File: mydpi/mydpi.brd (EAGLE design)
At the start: 41 x 20 mm, 35 parts, among them Q1 DMN3404L, U1 MEGA32U4-MU, U2 RT9193-33GB, Y1 830069392

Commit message: Minor changes placement
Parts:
- removed C6: 100n, zaan-Capacitors:C0603
- moved Q1 3.54 mm to (31.8, 12.2), turned to 90 degrees
- moved R4 3.26 mm to (32.5, 15.8), turned to 270 degrees
- moved SJ1 2.69 mm to (10.5, 28.5), turned to 180 degrees
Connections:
- removed net MEDBG_VTG: DBG1.4, SJ1.2
- new net VTG: C10.1, C11.1, C7.1, DBG1.4, SJ1.2
- net +3V3: no longer C10.1, C11.1
- net +5V: no longer C6.1, C7.1
- net GND: no longer C6.2
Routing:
- net PE6: track 19.5 -> 2.94 mm, vias 2 -> 1
- net MEDBG_UPDI: track 4.63 -> 0.00 mm
- net +3V3: track 3.74 -> 0.00 mm
- net VTG: track 0.00 -> 3.64 mm
- net GND: track 48.2 -> 46.0 mm, vias 30 -> 28
- net N$3: track 1.50 -> 0.00 mm

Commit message: Bugfixes in used libraries
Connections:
- removed net MEDBG_UPDI: DBG1.3, R4.2
- new net N$3: R4.2
- new net UDPI: DBG1.3
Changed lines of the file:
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@@
 </attributes>
 <variantdefs>
+<variantdef name="BOM"/>
 </variantdefs>
 <classes>
@@
 <attribute name="VOLTAGE" value="75V" x="25.75" y="16" size="1.778" layer="27" rot="R90" display="off"/>
 </element>
-<element name="ICSP1" library="zaan-Connectors" library_urn="urn:adsk.eagle:library:16759010" package="AVRISP-1.27-SMD" value="AVR-ISP-SMD" x="14.5" y="5.5" smashed="yes" rot="MR180">
+<element name="ICSP1" library="zaan-Connectors" library_urn="urn:adsk.eagle:library:16759010" package="AVRISP-1.27-SMD" package3d_urn="urn:adsk.eagle:package:17075154/1" value="AVR-ISP-SMD" x="14.5" y="5.5" smashed="yes" rot="MR180">
 <attribute name="NAME" x="17" y="5.5" size="1.016" layer="26" font="vector" ratio="15" rot="MR90" align="center"/>
 </element>
@@
 </element>
 <element name="Y1" library="zaan-Electromechanical" library_urn="urn:adsk.eagle:library:16759157" package="WE-XTAL_CFPX-218" package3d_urn="urn:adsk.eagle:package:16759170/1" value="830069392" x="22.5" y="2.75" smashed="yes" rot="R180">
+<attribute name="DESCRIPTION" value="Crystal" x="22.5" y="2.75" size="1.778" layer="27" rot="R180" display="off"/>
+<attribute name="MF" value="Wurth Electronics" x="22.5" y="2.75" size="1.778" layer="27" rot="R180" display="off"/>
+<attribute name="MPN" value="830069392" x="22.5" y="2.75" size="1.778" layer="27" rot="R180" display="off"/>
 <attribute name="NAME" x="22.5" y="5" size="1.016" layer="25" font="vector" ratio="15" align="center"/>
+<attribute name="PACKAGE" value="2520" x="22.5" y="2.75" size="1.778" layer="27" rot="R180" display="off"/>
 <attribute name="VALUE" x="22.5" y="5.25" size="1.016" layer="27" font="vector" ratio="15" rot="R180" align="center"/>
 </element>
@@
 </element>
 <element name="S1" library="zaan-Electromechanical" library_urn="urn:adsk.eagle:library:16759157" package="SPST-6X3.6" package3d_urn="urn:adsk.eagle:package:16760026/2" value="TS-1101-C-W" x="29.75" y="5.75" smashed="yes" rot="R270">
+<attribute name="DESCRIPTION" value="Tactile Button" x="29.75" y="5.75" size="1.778" layer="27" rot="R270" display="off"/>
+<attribute name="MF" value="Korean Hroparts Elec" x="29.75" y="5.75" size="1.778" layer="27" rot="R270" display="off"/>
+<attribute name="MPN" value="K2-1107ST-A4SW-06" x="29.75" y="5.75" size="1.778" layer="27" rot="R270" display="off"/>
 <attribute name="NAME" x="28.25" y="9.75" size="1.016" layer="25" font="vector" ratio="15" rot="R270" align="center"/>
+<attribute name="PACKAGE" value="6.1X3.6X2.5" x="29.75" y="5.75" size="1.778" layer="27" rot="R270" display="off"/>
 <attribute name="VALUE" x="27.25" y="5.75" size="1.016" layer="27" font="vector" ratio="15" rot="R270" align="center"/>
 </element>
@@
 <attribute name="MPN" value="MF-PSMF035X-2" x="9.25" y="6.5" size="1.778" layer="27" rot="R270" display="off"/>
 <attribute name="NAME" x="9.25" y="4" size="1.016" layer="25" font="vector" ratio="15" rot="R270" align="center"/>
-<attribute name="PACKAGE" value="0805" x="9.25" y="6.5" size="1.778" layer="27" rot="R270" display="off"/>
+<attribute name="PACKAGE" value="2012" x="9.25" y="6.5" size="1.778" layer="27" rot="R270" display="off"/>
 <attribute name="VALUE" x="5.75" y="6.5" size="1.016" layer="27" font="vector" ratio="15" rot="R270" align="center"/>
 </element>
@@
 <wire x1="8.5" y1="14.65" x2="7.5" y2="14.65" width="0.254" layer="1"/>
 <via x="7.5" y="14.65" extent="1-16" drill="0.3"/>
+<wire x1="33.25" y1="7.25" x2="38.77" y2="11.905" width="0" layer="19" extent="1-1"/>
+<wire x1="29.75" y1="8.25" x2="32.25" y2="7.25" width="0" layer="19" extent="1-1"/>
+<wire x1="27.5" y1="7.25" x2="29.75" y2="8.25" width="0" layer="19" extent="1-1"/>
+<wire x1="20.5" y1="10" x2="22.75" y2="7.75" width="0" layer="19" extent="1-1"/>
+<wire x1="22.5" y1="12" x2="20.5" y2="10" width="0" layer="19" extent="1-1"/>
+<wire x1="19.5" y1="17" x2="21.5" y2="17" width="0" layer="19" extent="1-1"/>
+<wire x1="17.025" y1="10.5" x2="18.5" y2="12" width="0" layer="19" extent="1-1"/>
+<wire x1="21.5375" y1="3.5125" x2="19.498" y2="5.75" width="0" layer="19" extent="1-1"/>
+<wire x1="22.5125" y1="1.9875" x2="22.4875" y2="3.5125" width="0" layer="19" extent="1-1"/>
+<wire x1="25.5" y1="1.9" x2="23.4625" y2="1.9875" width="0" layer="19" extent="1-1"/>
+<wire x1="19.5" y1="1.9" x2="21.5375" y2="3.5125" width="0" layer="19" extent="1-1"/>
+<wire x1="17.5" y1="1.9" x2="19.5" y2="1.9" width="0" layer="19" extent="1-1"/>
+<wire x1="15.5" y1="2.75" x2="17.5" y2="1.9" width="0" layer="19" extent="1-1"/>
+<wire x1="15.135" y1="6.77" x2="15.5" y2="3.65" width="0" layer="19" extent="1-16"/>
+<wire x1="14.5" y1="13.75" x2="15.75" y2="10.398" width="0" layer="19" extent="1-1"/>
+<wire x1="11.25" y1="15.5" x2="14.5" y2="14.65" width="0" layer="19" extent="1-1"/>
+<wire x1="8.5" y1="14.65" x2="10.21" y2="15.5" width="0" layer="19" extent="1-1"/>
+<wire x1="7.725" y1="13.225" x2="7.5" y2="14.65" width="0" layer="19" extent="1-1"/>
+<wire x1="6.25" y1="16" x2="7.5" y2="14.65" width="0" layer="19" extent="1-1"/>
+<wire x1="12.75" y1="18" x2="11.25" y2="15.5" width="0" layer="19" extent="1-1"/>
+<wire x1="11.25" y1="6.15" x2="15.135" y2="6.77" width="0" layer="19" extent="1-16"/>
+<wire x1="7.725" y1="6.775" x2="11.25" y2="6.15" width="0" layer="19" extent="1-1"/>
+<wire x1="6.25" y1="4" x2="6.51" y2="6.775" width="0" layer="19" extent="1-1"/>
+<wire x1="6.5" y1="1.75" x2="6.25" y2="4" width="0" layer="19" extent="1-1"/>
+<wire x1="1.95" y1="18.5" x2="5.35" y2="16" width="0" layer="19" extent="1-1"/>
 </signal>
 <signal name="+5V">
@@
 <wire x1="14.5" y1="3.595" x2="14.5" y2="3.23" width="0.254" layer="16"/>
 <via x="14.5" y="3.23" extent="1-16" drill="0.3"/>
-<wire x1="8.35" y1="18.5" x2="13" y2="28" width="0" layer="19" extent="1-1"/>
+<wire x1="25.75" y1="16.85" x2="29.75" y2="14.95" width="0" layer="19" extent="1-1"/>
+<wire x1="23.6" y1="16" x2="25.75" y2="16.85" width="0" layer="19" extent="1-1"/>
+<wire x1="19" y1="13.475" x2="23" y2="13.475" width="0" layer="19" extent="1-1"/>
+<wire x1="18" y1="13.475" x2="19" y2="13.475" width="0" layer="19" extent="1-1"/>
+<wire x1="17.025" y1="12" x2="18" y2="13.475" width="0" layer="19" extent="1-1"/>
+<wire x1="17.025" y1="9.5" x2="17.025" y2="12" width="0" layer="19" extent="1-1"/>
+<wire x1="19" y1="6.525" x2="17.025" y2="9.5" width="0" layer="19" extent="1-1"/>
+<wire x1="17.5" y1="3.6" x2="19" y2="6.525" width="0" layer="19" extent="1-1"/>
+<wire x1="15.135" y1="4.23" x2="17.5" y2="3.6" width="0" layer="19" extent="1-16"/>
+<wire x1="13.5" y1="3.65" x2="14.5" y2="3.23" width="0" layer="19" extent="1-1"/>
+<wire x1="9.45" y1="1.75" x2="13.5" y2="3.65" width="0" layer="19" extent="1-1"/>
+<wire x1="9.25" y1="5.5" x2="9.45" y2="1.75" width="0" layer="19" extent="1-1"/>
+<wire x1="23.975" y1="8" x2="19" y2="6.525" width="0" layer="19" extent="1-1"/>
+<wire x1="10.21" y1="16.45" x2="17.4" y2="16" width="0" layer="19" extent="1-1"/>
+<wire x1="8.5" y1="16.35" x2="10.21" y2="16.45" width="0" layer="19" extent="1-1"/>
+<wire x1="8.35" y1="18.5" x2="8.5" y2="16.35" width="0" layer="19" extent="1-1"/>
+<wire x1="13" y1="28" x2="8.35" y2="18.5" width="0" layer="19" extent="1-1"/>
 </signal>
 <signal name="N$1">
@@
 <wire x1="8" y1="10.25" x2="8" y2="9.5" width="0.254" layer="1"/>
 </signal>
-<signal name="MEDBG_UPDI">
-<contactref element="DBG1" pad="3"/>
-<contactref element="R4" pad="2"/>
-<wire x1="32.5" y1="14.9" x2="36.23" y2="10.635" width="0" layer="19" extent="1-1"/>
-</signal>
 <signal name="+3V3">
 <contactref element="SJ1" pad="1"/>
@@
 <contactref element="ICSP1" pad="1"/>
 <wire x1="13.865" y1="4.23" x2="14.508" y2="4.873" width="0.254" layer="16"/>
-<wire x1="15.873" y1="4.873" x2="16" y2="5" width="0.254" layer="16"/>
+<wire x1="15.623" y1="4.873" x2="16" y2="5.25" width="0.254" layer="16"/>
 <via x="16" y="7" extent="1-16" drill="0.3"/>
 <wire x1="16" y1="7" x2="16.5" y2="7.5" width="0.254" layer="1"/>
 <wire x1="16.5" y1="7.5" x2="17.025" y2="7.5" width="0.254" layer="1"/>
-<wire x1="14.508" y1="4.873" x2="15.873" y2="4.873" width="0.254" layer="16"/>
-<wire x1="16" y1="5" x2="16" y2="7" width="0.254" layer="16"/>
+<wire x1="14.508" y1="4.873" x2="15.623" y2="4.873" width="0.254" layer="16"/>
+<wire x1="16" y1="5.25" x2="16" y2="7" width="0.254" layer="16"/>
 </signal>
 <signal name="RST">
@@
 <wire x1="12" y1="28.5" x2="15.35" y2="18" width="0" layer="19" extent="1-16"/>
 </signal>
+<signal name="UDPI">
+<contactref element="DBG1" pad="3"/>
+</signal>
+<signal name="N$3">
+<contactref element="R4" pad="2"/>
+</signal>
 </signals>

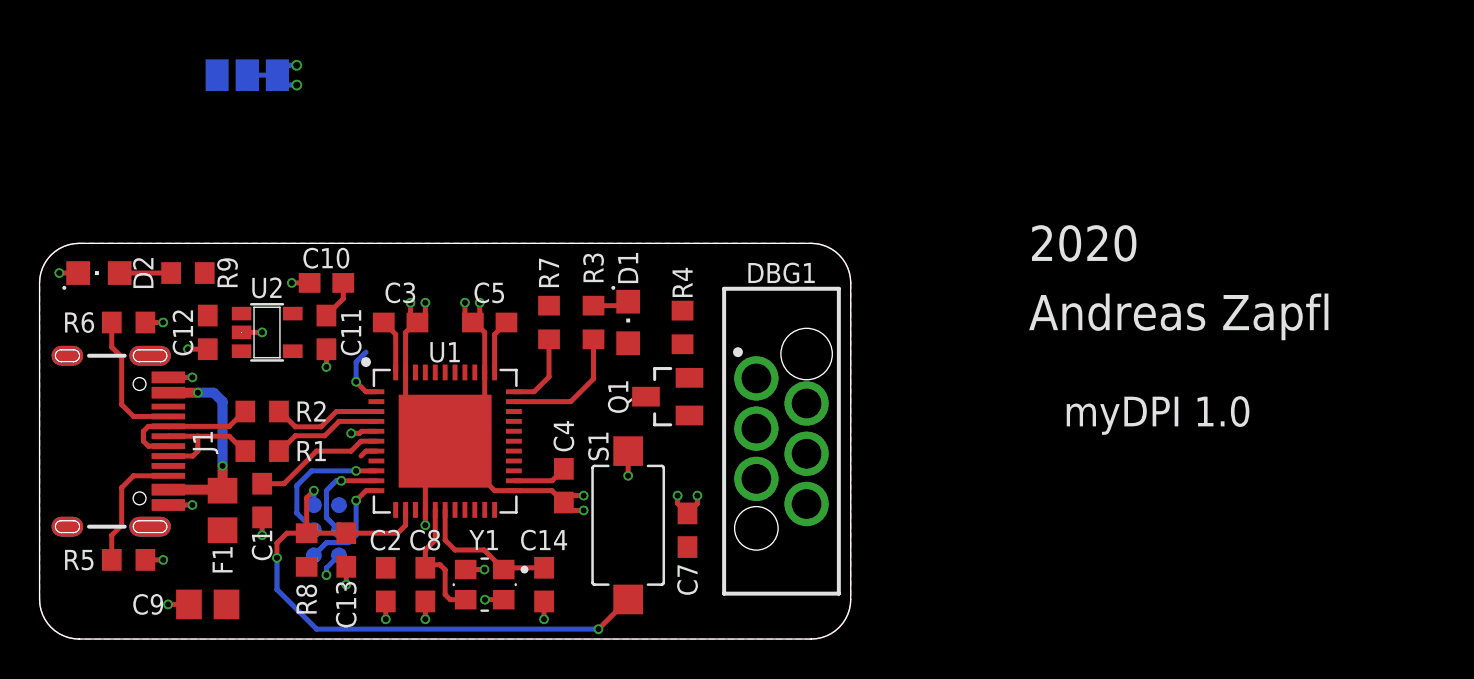
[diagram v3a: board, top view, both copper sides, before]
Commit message: Finished level shifter
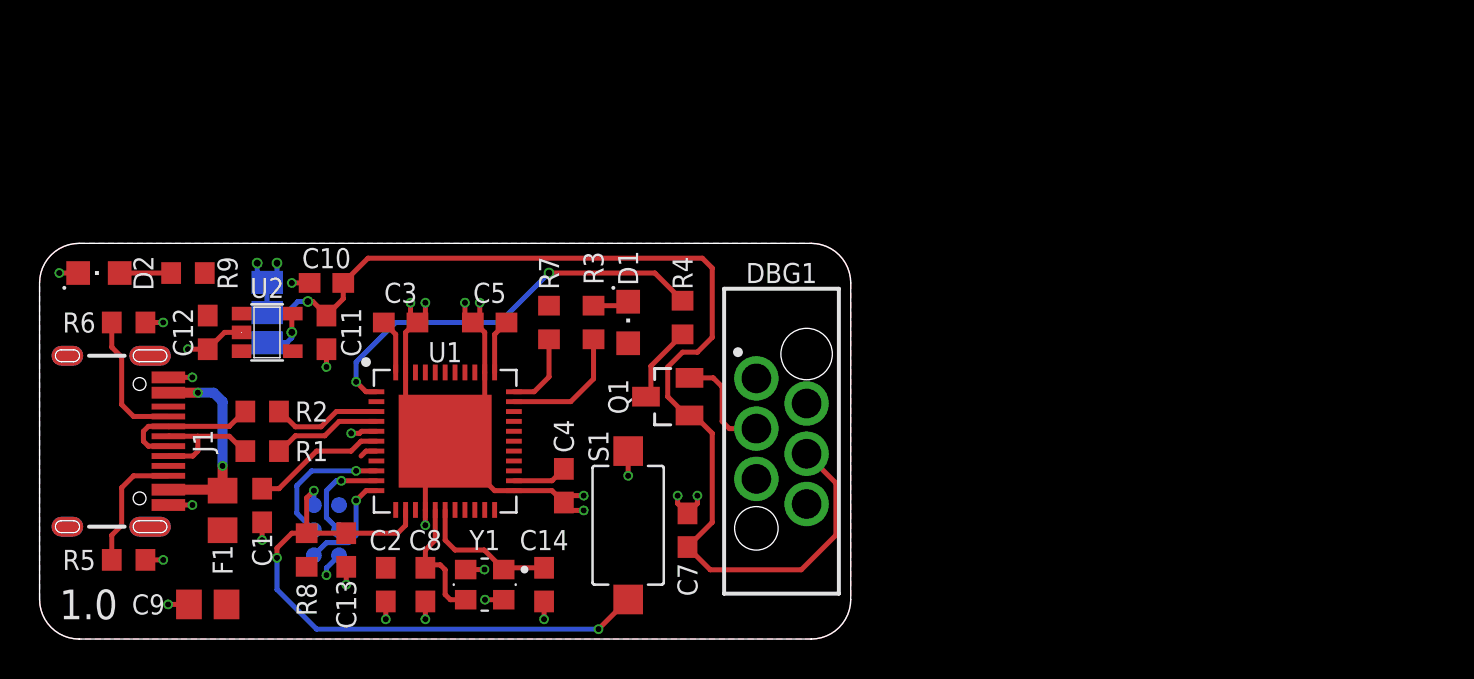
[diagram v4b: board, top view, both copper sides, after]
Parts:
- moved SJ1 12.0 mm to (11.5, 16.5), turned to 90 degrees
- moved R4 0.50 mm to (32.5, 16.2)
- moved C1 0.25 mm to (11.2, 6.75)
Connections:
- removed net N$10: Q1.3
- removed net N$11: Q1.2
- removed net N$3: R4.2
- removed net N$4: Q1.1
- new net UDPI_RAW: Q1.3, R4.2
- net UDPI: now also Q1.2
- net VTG: now also Q1.1
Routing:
- net VTG: track 3.64 -> 57.0 mm, vias 0 -> 1
- net PE6: track 2.94 -> 21.2 mm, vias 1 -> 2
- net UDPI: track 0.00 -> 5.47 mm
- net UDPI_RAW: track 0.00 -> 3.92 mm
- net +3V3: track 0.00 -> 2.60 mm, vias 0 -> 1
- net GND: track 46.0 -> 47.0 mm, vias 28 -> 27
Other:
- board text added: "1.0"

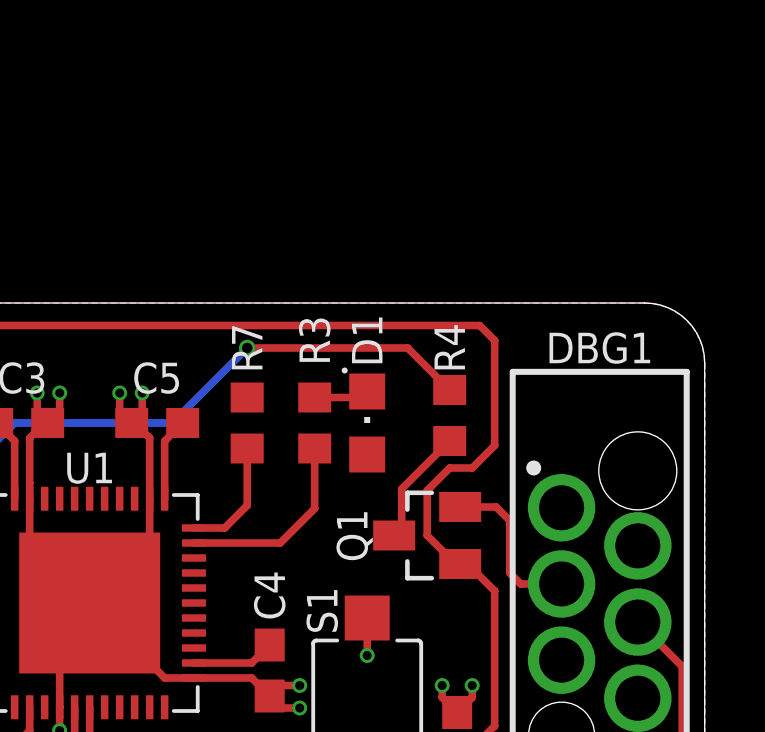
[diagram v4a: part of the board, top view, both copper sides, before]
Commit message: Added pullup resistors for level shifting
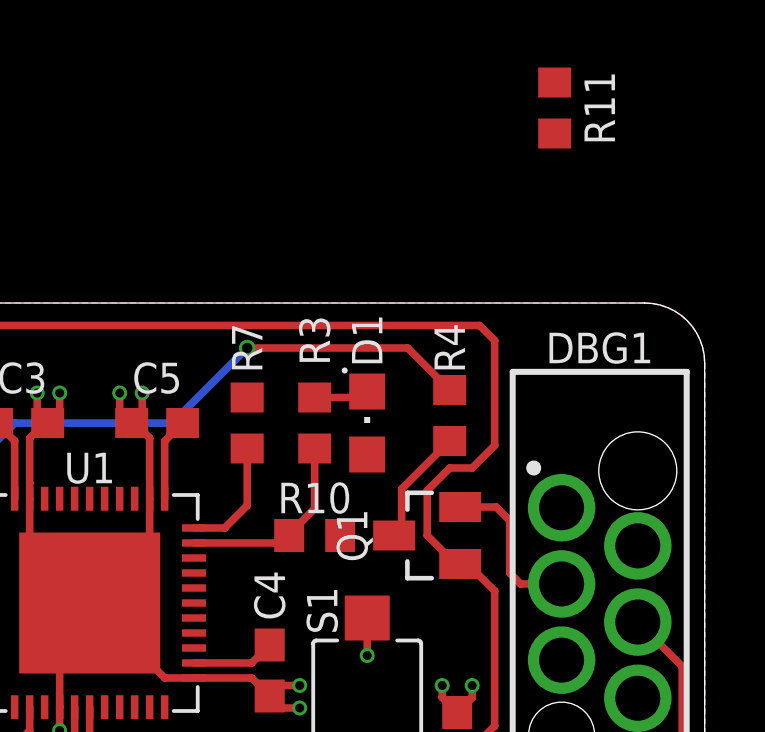
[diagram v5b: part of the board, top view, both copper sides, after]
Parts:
- added R10, R11: 4.7k, zaan-Resistors:R0603
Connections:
- net +5V: now also R10.2
- net UDPI: now also R11.1
- net UDPI_RAW: now also R10.1
- net VTG: now also R11.2
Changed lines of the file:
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@@
 <drawing>
 <settings>
-<setting alwaysvectorfont="yes"/>
+<setting alwaysvectorfont="no"/>
 <setting verticaltext="up"/>
 </settings>
@@
 <attribute name="VALUE" x="34.25" y="12.25" size="1.016" layer="27" font="vector" ratio="15" rot="R90" align="center"/>
 </element>
+<element name="R10" library="zaan-Resistors" library_urn="urn:adsk.eagle:library:16759442" package="R0603" package3d_urn="urn:adsk.eagle:package:16759452/1" value="4.7k" x="28" y="12.25" smashed="yes" rot="R180">
+<attribute name="DESCRIPTION" value="Surface Mount Resistor" x="28" y="12.25" size="1.778" layer="27" rot="R180" display="off"/>
+<attribute name="MF" value="Yageo" x="28" y="12.25" size="1.778" layer="27" rot="R180" display="off"/>
+<attribute name="MPN" value="RC0603FR-074K7L" x="28" y="12.25" size="1.778" layer="27" rot="R180" display="off"/>
+<attribute name="NAME" x="28" y="13.5" size="1.016" layer="25" font="vector" ratio="15" rot="R180" align="center"/>
+<attribute name="PACKAGE" value="1608" x="28" y="12.25" size="1.778" layer="27" rot="R180" display="off"/>
+<attribute name="PACKAGE-IN" value="0603" x="28" y="12.25" size="1.778" layer="27" rot="R180" display="off"/>
+<attribute name="POWER" value="0.1W" x="28" y="12.25" size="1.778" layer="27" rot="R180" display="off"/>
+<attribute name="TOLERANCE" value="1%" x="28" y="12.25" size="1.778" layer="27" rot="R180" display="off"/>
+<attribute name="VALUE" x="28" y="13.75" size="1.016" layer="27" font="vector" ratio="15" rot="R180" align="center"/>
+<attribute name="VOLTAGE" value="75V" x="28" y="12.25" size="1.778" layer="27" rot="R180" display="off"/>
+</element>
+<element name="R11" library="zaan-Resistors" library_urn="urn:adsk.eagle:library:16759442" package="R0603" package3d_urn="urn:adsk.eagle:package:16759452/1" value="4.7k" x="36" y="26.5" smashed="yes" rot="R270">
+<attribute name="DESCRIPTION" value="Surface Mount Resistor" x="36" y="26.5" size="1.778" layer="27" rot="R270" display="off"/>
+<attribute name="MF" value="Yageo" x="36" y="26.5" size="1.778" layer="27" rot="R270" display="off"/>
+<attribute name="MPN" value="RC0603FR-074K7L" x="36" y="26.5" size="1.778" layer="27" rot="R270" display="off"/>
+<attribute name="NAME" x="37.5" y="26.5" size="1.016" layer="25" font="vector" ratio="15" rot="R270" align="center"/>
+<attribute name="PACKAGE" value="1608" x="36" y="26.5" size="1.778" layer="27" rot="R270" display="off"/>
+<attribute name="PACKAGE-IN" value="0603" x="36" y="26.5" size="1.778" layer="27" rot="R270" display="off"/>
+<attribute name="POWER" value="0.1W" x="36" y="26.5" size="1.778" layer="27" rot="R270" display="off"/>
+<attribute name="TOLERANCE" value="1%" x="36" y="26.5" size="1.778" layer="27" rot="R270" display="off"/>
+<attribute name="VALUE" x="34.5" y="26.5" size="1.016" layer="27" font="vector" ratio="15" rot="R270" align="center"/>
+<attribute name="VOLTAGE" value="75V" x="36" y="26.5" size="1.778" layer="27" rot="R270" display="off"/>
+</element>
 </elements>
 <signals>
@@
 <wire x1="14.5" y1="3.595" x2="14.5" y2="3.23" width="0.254" layer="16"/>
 <via x="14.5" y="3.23" extent="1-16" drill="0.3"/>
+<contactref element="R10" pad="2"/>
 </signal>
 <signal name="N$1">
@@
 <wire x1="30.9" y1="13.8" x2="30.9" y2="12.5" width="0.254" layer="1"/>
 <wire x1="32.5" y1="15.4" x2="30.9" y2="13.8" width="0.254" layer="1"/>
+<contactref element="R10" pad="1"/>
+<wire x1="28.85" y1="12.25" x2="30.65" y2="12.25" width="0" layer="19" extent="1-1"/>
 </signal>
 <signal name="N$12">
@@
 <wire x1="31.75" y1="12.25" x2="31.75" y2="13.75" width="0.254" layer="1"/>
 <wire x1="34" y1="15.25" x2="34" y2="18.75" width="0.254" layer="1"/>
+<contactref element="R11" pad="2"/>
+<wire x1="32.85" y1="11.3" x2="36" y2="25.65" width="0" layer="19" extent="1-1"/>
 <wire x1="14.5" y1="16.37033125" x2="14.5" y2="16.35" width="0" layer="19" extent="1-1"/>
 </signal>
@@
 <wire x1="34.05" y1="13.2" x2="34.5" y2="12.75" width="0.254" layer="1"/>
 <wire x1="34.5" y1="12.75" x2="34.5" y2="11" width="0.254" layer="1"/>
+<contactref element="R11" pad="1"/>
+<wire x1="32.85" y1="13.2" x2="36" y2="27.35" width="0" layer="19" extent="1-1"/>
 </signal>
 </signals>
